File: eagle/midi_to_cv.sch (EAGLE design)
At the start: 35 parts, among them IC2 4504N, IC3 4099N, U1 ATMEGA328P_PDIP

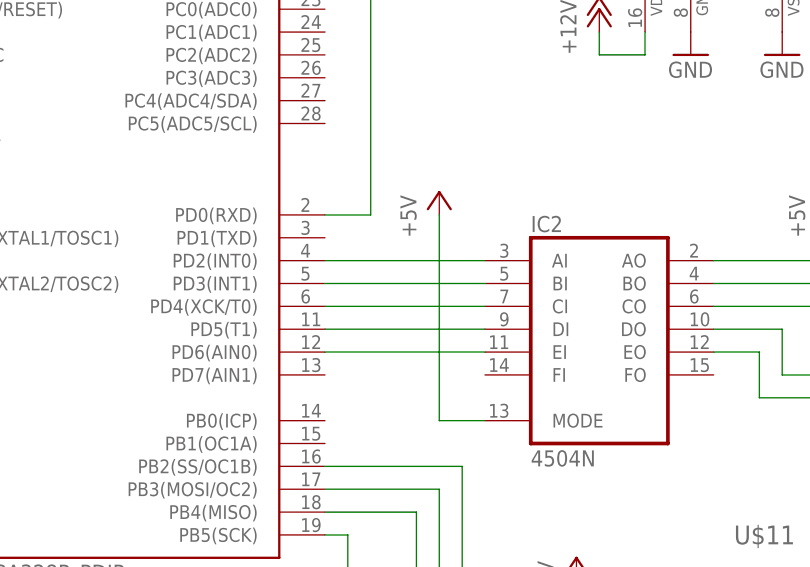
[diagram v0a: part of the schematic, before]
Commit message: starting brd and dac library
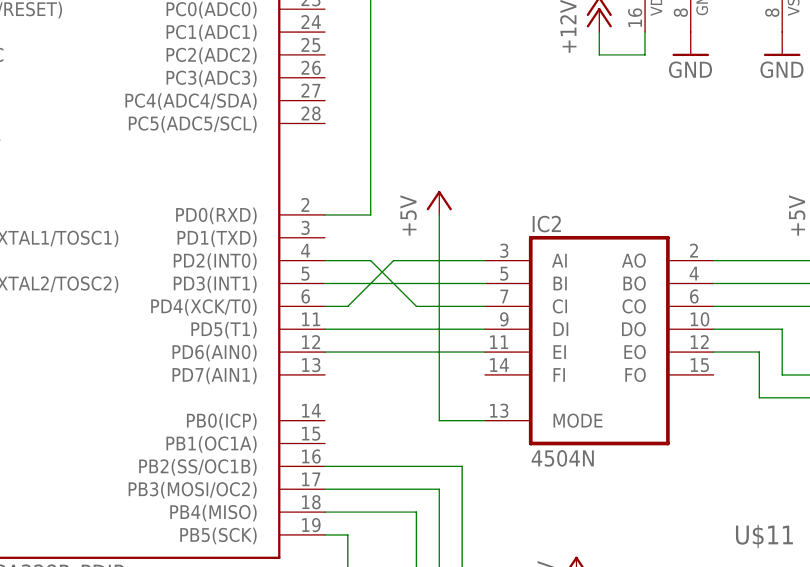
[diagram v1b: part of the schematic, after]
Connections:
- net N$23: now also U1.PD2(INT0); no longer U1.PD4(XCK/T0)
- net N$25: now also U1.PD4(XCK/T0); no longer U1.PD2(INT0)
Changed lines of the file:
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@@
-</segment>
-</net>
-<net name="N$23" class="0">
-<segment>
-<pinref part="U1" gate="G$1" pin="PD4(XCK/T0)"/>
-<wire x1="43.18" y1="40.64" x2="60.96" y2="40.64" width="0.1524" layer="91"/>
-<pinref part="IC2" gate="A" pin="CI"/>
-</segment>
-</net>
-<net name="N$25" class="0">
-<segment>
-<pinref part="U1" gate="G$1" pin="PD2(INT0)"/>
-<wire x1="43.18" y1="45.72" x2="60.96" y2="45.72" width="0.1524" layer="91"/>
-<pinref part="IC2" gate="A" pin="AI"/>
 </segment>
 </net>
@@
 </segment>
 </net>
+<net name="N$23" class="0">
+<segment>
+<pinref part="U1" gate="G$1" pin="PD2(INT0)"/>
+<wire x1="43.18" y1="45.72" x2="48.26" y2="45.72" width="0.1524" layer="91"/>
+<wire x1="48.26" y1="45.72" x2="53.34" y2="40.64" width="0.1524" layer="91"/>
+<pinref part="IC2" gate="A" pin="CI"/>
+<wire x1="53.34" y1="40.64" x2="60.96" y2="40.64" width="0.1524" layer="91"/>
+</segment>
+</net>
+<net name="N$25" class="0">
+<segment>
+<pinref part="U1" gate="G$1" pin="PD4(XCK/T0)"/>
+<wire x1="43.18" y1="40.64" x2="45.72" y2="40.64" width="0.1524" layer="91"/>
+<wire x1="45.72" y1="40.64" x2="50.8" y2="45.72" width="0.1524" layer="91"/>
+<pinref part="IC2" gate="A" pin="AI"/>
+<wire x1="50.8" y1="45.72" x2="60.96" y2="45.72" width="0.1524" layer="91"/>
+</segment>
+</net>

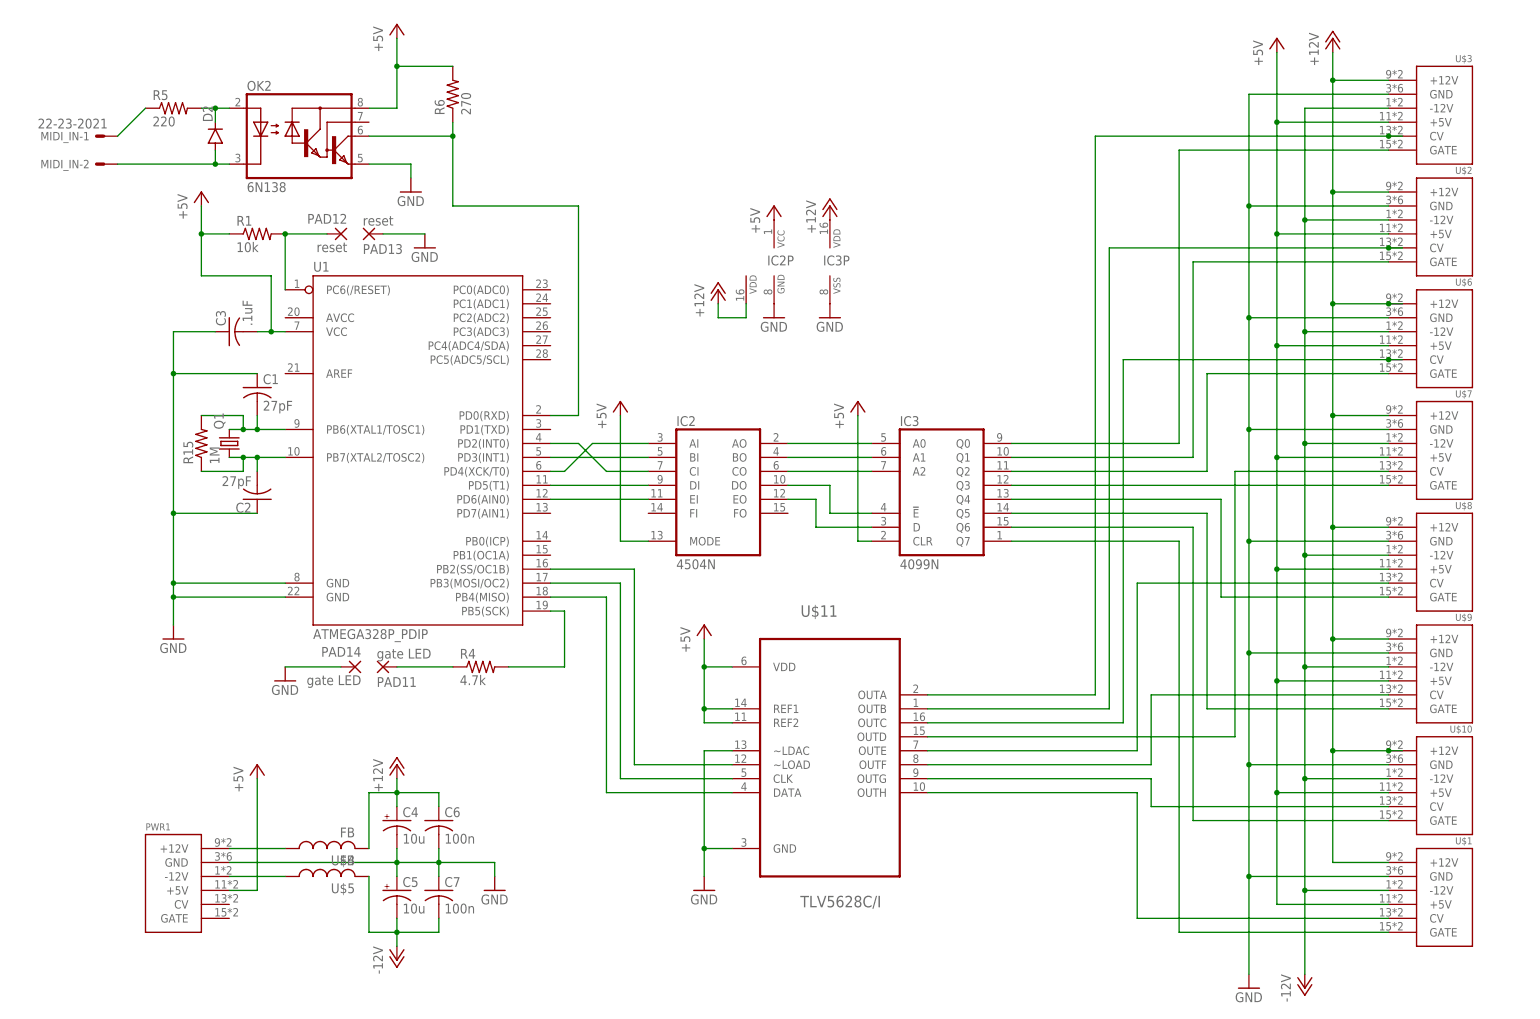
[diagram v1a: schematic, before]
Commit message: adding output resistors
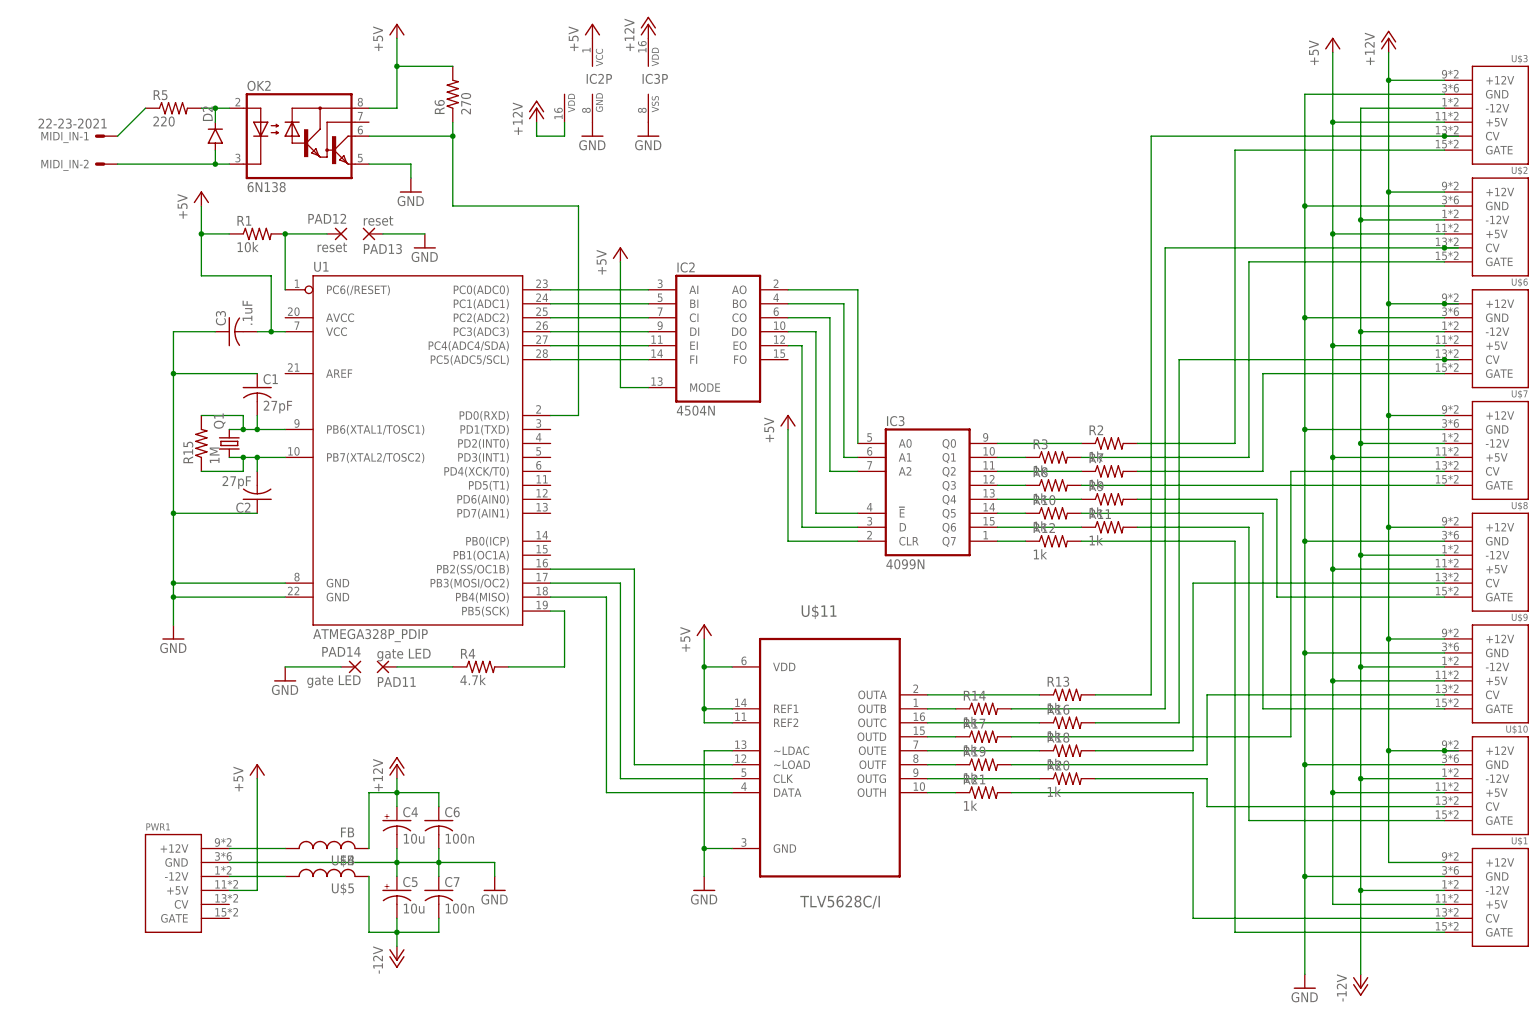
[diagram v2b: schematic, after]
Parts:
- added R10, R11, R12, R13, R14, R16, R17, R18, R19, R2, R20, R21, R3, R7, R8, R9: 1k, rcl:R-US_0207/10
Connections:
- new net N$43: IC2A.FI, U1.PC5(ADC5/SCL)
- new net N$44: IC3A.Q1, R3.1
- new net N$45: IC3A.Q2, R7.1
- new net N$46: IC3A.Q3, R8.1
- new net N$47: IC3A.Q4, R9.1
- new net N$48: IC3A.Q5, R10.1
- new net N$49: IC3A.Q6, R11.1
- new net N$50: IC3A.Q7, R12.1
- new net N$51: R8.2, U$7.GATE
- new net N$52: R13.1, U$11.OUTA
- new net N$53: R14.1, U$11.OUTB
- new net N$54: R16.1, U$11.OUTC
- new net N$55: R17.1, U$11.OUTD
- new net N$56: R18.1, U$11.OUTE
- new net N$57: R19.1, U$11.OUTF
- new net N$58: R20.1, U$11.OUTG
- new net N$59: R21.1, U$11.OUTH
- net N$12: now also R11.2; no longer IC3A.Q6
- net N$16: now also R12.2; no longer IC3A.Q7
- net N$21: now also R17.2; no longer U$11.OUTD
- net N$22: now also R18.2; no longer U$11.OUTE
- net N$23: now also IC2A.AI, U1.PC0(ADC0); no longer IC2A.CI, U1.PD2(INT0)
- net N$24: now also R19.2; no longer U$11.OUTF
- net N$25: now also IC2A.BI, U1.PC1(ADC1); no longer IC2A.AI, U1.PD4(XCK/T0)
- net N$28: now also R20.2; no longer U$11.OUTG
- net N$29: now also R21.2; no longer U$11.OUTH
- net N$3: now also R13.2; no longer U$11.OUTA
- net N$31: now also IC2A.CI, U1.PC2(ADC2); no longer IC2A.BI, U1.PD3(INT1)
- net N$32: now also IC2A.DI, U1.PC3(ADC3); no longer IC2A.EI, U1.PD6(AIN0)
- net N$34: now also IC2A.EI, U1.PC4(ADC4/SDA); no longer IC2A.DI, U1.PD5(T1)
- net N$39: now also IC3A.Q0, R2.1; no longer IC3A.Q3, U$7.GATE
- net N$40: now also R7.2; no longer IC3A.Q2
- net N$41: now also R3.2; no longer IC3A.Q1
- net N$42: now also R2.2; no longer IC3A.Q0
- net N$6: now also R9.2; no longer IC3A.Q4
- net N$7: now also R14.2; no longer U$11.OUTB
- net N$8: now also R16.2; no longer U$11.OUTC
- net N$9: now also R10.2; no longer IC3A.Q5
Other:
- moved on the sheet: IC2, IC2P, IC3, IC3P, U$1, U$10, U$2, U$3, U$6, U$7, U$8, U$9

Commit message: ribbon connectors with interleaved gate cna cv instead of power connectors
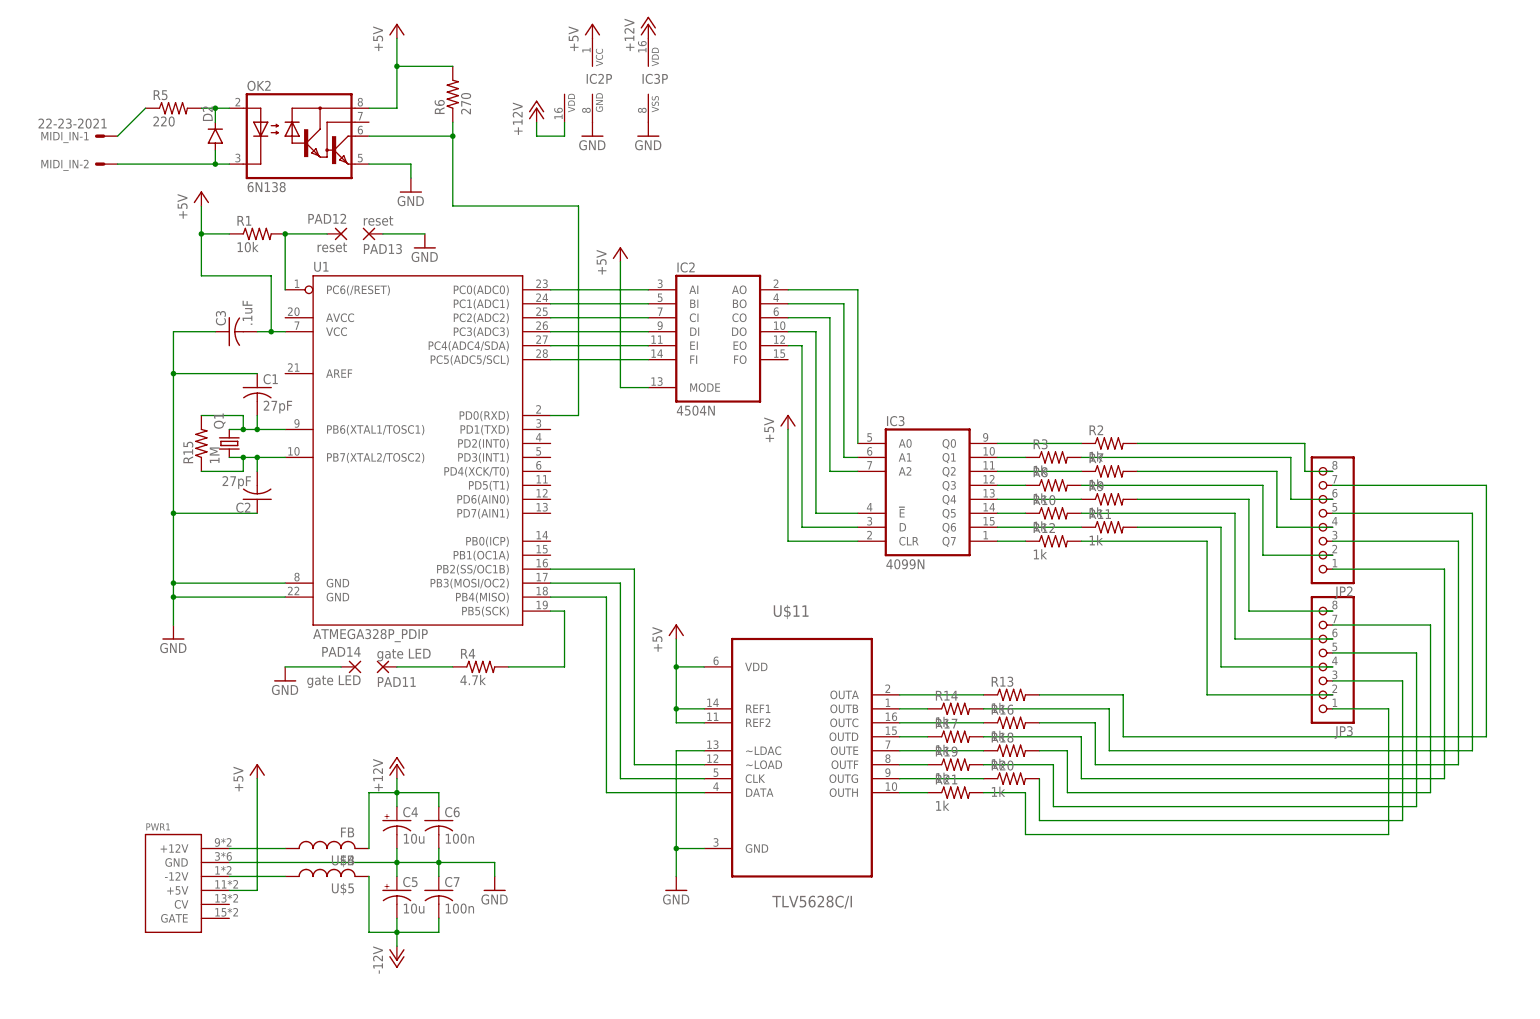
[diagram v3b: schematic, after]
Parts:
- removed U$1, U$10, U$2, U$3, U$6, U$7, U$8, U$9: POWER, eurorack:POWER
- added JP2, JP3: (no value), pinhead:PINHD-1X8
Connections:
- net +12V: no longer U$1.+12V, U$10.+12V, U$2.+12V, U$3.+12V, U$6.+12V, U$7.+12V, U$8.+12V, U$9.+12V
- net +5V: no longer U$1.+5V, U$10.+5V, U$2.+5V, U$3.+5V, U$6.+5V, U$7.+5V, U$8.+5V, U$9.+5V
- net -12V: no longer U$1.-12V, U$10.-12V, U$2.-12V, U$3.-12V, U$6.-12V, U$7.-12V, U$8.-12V, U$9.-12V
- net GND: no longer U$1.GND, U$10.GND, U$2.GND, U$3.GND, U$6.GND, U$7.GND, U$8.GND, U$9.GND
- net N$12: now also JP3.6, R10.2; no longer R11.2, U$10.GATE
- net N$16: now also JP3.4, R11.2; no longer R12.2, U$1.GATE
- net N$21: now also JP3.2, R12.2; no longer R17.2, U$7.CV
- net N$22: now also JP2.7, R13.2; no longer R18.2, U$8.CV
- net N$24: now also JP2.5, R14.2; no longer R19.2, U$9.CV
- net N$28: now also JP2.3, R16.2; no longer R20.2, U$10.CV
- net N$29: now also JP2.1, R17.2; no longer R21.2, U$1.CV
- net N$3: now also JP2.8, R2.2; no longer R13.2, U$3.CV
- net N$40: now also JP3.7, R18.2; no longer R7.2, U$6.GATE
- net N$41: now also JP3.5, R19.2; no longer R3.2, U$2.GATE
- net N$42: now also JP3.3, R20.2; no longer R2.2, U$3.GATE
- net N$51: now also JP3.1, R21.2; no longer R8.2, U$7.GATE
- net N$6: now also JP2.6, R3.2; no longer R9.2, U$8.GATE
- net N$7: now also JP2.4, R7.2; no longer R14.2, U$2.CV
- net N$8: now also JP2.2, R8.2; no longer R16.2, U$6.CV
- net N$9: now also JP3.8, R9.2; no longer R10.2, U$9.GATE
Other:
- moved on the sheet: R13, R14, R16, R17, R18, R19, R20, R21, U$11
